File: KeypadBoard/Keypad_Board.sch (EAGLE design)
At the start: 31 parts, among them Q1 4.3A/20V/54mΩ, U1 ESP32-WROOM-32E_(16MB), U2 LTC1730ES8-4.2#TRPBF

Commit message: Board Rev2
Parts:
- added J8: (no value), SparkFun-Connectors:CONN_05
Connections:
- new net BTN1: J8.3, U1.IO15
- new net X_AXIS: J8.5, U1.IO34
- new net Y_AXIS: J8.4, U1.IO35
- net 3V3: now also J8.1
- net GND: now also J8.2
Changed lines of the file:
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@@
 <part name="SUPPLY10" library="supply2" library_urn="urn:adsk.eagle:library:372" deviceset="GND" device=""/>
 <part name="J7" library="SparkFun-Connectors" library_urn="urn:adsk.eagle:library:513" deviceset="CONN_02" device="" package3d_urn="urn:adsk.eagle:package:38039/1"/>
+<part name="J8" library="SparkFun-Connectors" library_urn="urn:adsk.eagle:library:513" deviceset="CONN_05" device="" package3d_urn="urn:adsk.eagle:package:38104/1"/>
 </parts>
 <sheets>
@@
 <attribute name="NAME" x="66.04" y="104.648" size="1.778" layer="95" font="vector"/>
 </instance>
+<instance part="J8" gate="G$1" x="325.12" y="45.72" smashed="yes" rot="R180">
+<attribute name="VALUE" x="327.66" y="55.626" size="1.778" layer="96" font="vector" rot="R180"/>
+<attribute name="NAME" x="327.66" y="37.592" size="1.778" layer="95" font="vector" rot="R180"/>
+</instance>
 </instances>
 <busses>
@@
 <pinref part="SUPPLY10" gate="GND" pin="GND"/>
 <wire x1="294.64" y1="137.16" x2="294.64" y2="132.08" width="0.1524" layer="91"/>
+</segment>
+<segment>
+<pinref part="J8" gate="G$1" pin="2"/>
+<wire x1="317.5" y1="48.26" x2="307.34" y2="48.26" width="0.1524" layer="91"/>
+<label x="307.34" y="48.26" size="1.778" layer="95"/>
 </segment>
 </net>
@@
 <label x="271.78" y="83.82" size="1.778" layer="95"/>
 </segment>
+<segment>
+<pinref part="J8" gate="G$1" pin="1"/>
+<wire x1="317.5" y1="50.8" x2="307.34" y2="50.8" width="0.1524" layer="91"/>
+<label x="307.34" y="50.8" size="1.778" layer="95"/>
+</segment>
 </net>
 <net name="N$9" class="0">
@@
 </segment>
 </net>
+<net name="X_AXIS" class="0">
+<segment>
+<pinref part="J8" gate="G$1" pin="5"/>
+<wire x1="317.5" y1="40.64" x2="307.34" y2="40.64" width="0.1524" layer="91"/>
+<label x="307.34" y="40.64" size="1.778" layer="95"/>
+</segment>
+<segment>
+<pinref part="U1" gate="G$1" pin="IO34"/>
+<wire x1="233.68" y1="121.92" x2="223.52" y2="121.92" width="0.1524" layer="91"/>
+<label x="223.52" y="121.92" size="1.778" layer="95"/>
+</segment>
+</net>
+<net name="Y_AXIS" class="0">
+<segment>
+<pinref part="J8" gate="G$1" pin="4"/>
+<wire x1="317.5" y1="43.18" x2="307.34" y2="43.18" width="0.1524" layer="91"/>
+<label x="307.34" y="43.18" size="1.778" layer="95"/>
+</segment>
+<segment>
+<pinref part="U1" gate="G$1" pin="IO35"/>
+<wire x1="233.68" y1="119.38" x2="223.52" y2="119.38" width="0.1524" layer="91"/>
+<label x="223.52" y="119.38" size="1.778" layer="95"/>
+</segment>
+</net>
+<net name="BTN1" class="0">
+<segment>
+<pinref part="J8" gate="G$1" pin="3"/>
+<wire x1="317.5" y1="45.72" x2="307.34" y2="45.72" width="0.1524" layer="91"/>
+<label x="307.34" y="45.72" size="1.778" layer="95"/>
+</segment>
+<segment>
+<pinref part="U1" gate="G$1" pin="IO15"/>
+<wire x1="274.32" y1="132.08" x2="284.48" y2="132.08" width="0.1524" layer="91"/>
+<label x="276.86" y="132.08" size="1.778" layer="95"/>
+</segment>
+</net>

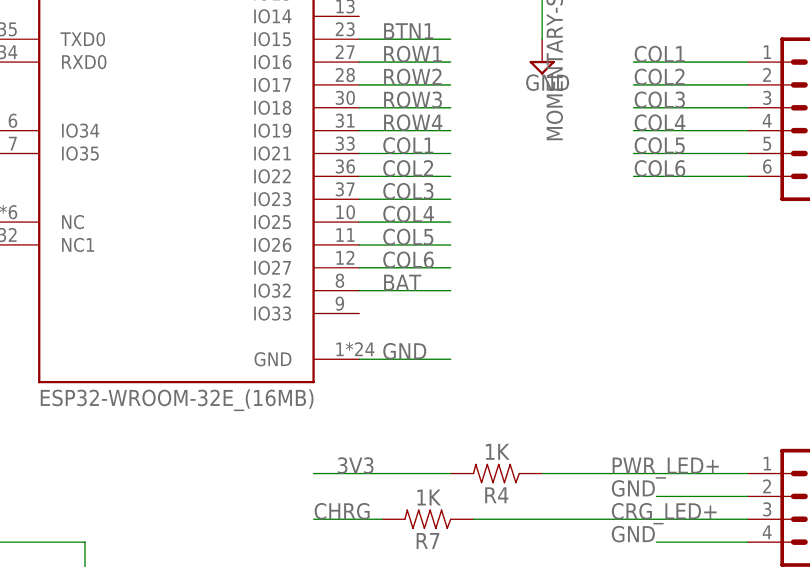
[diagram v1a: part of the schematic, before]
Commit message: Board updates - ADC OverVoltage fix
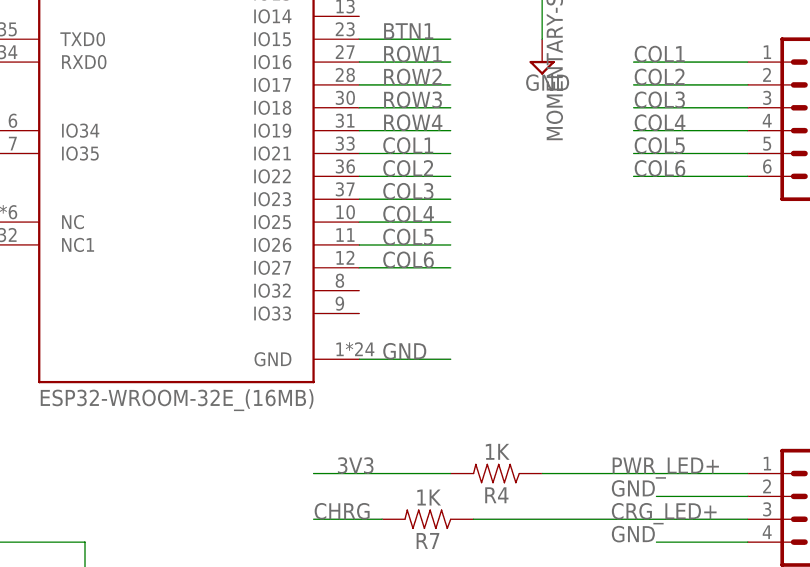
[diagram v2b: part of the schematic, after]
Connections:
- net BAT: no longer U1.IO32
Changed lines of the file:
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@@
 <net name="BAT" class="0">
-<segment>
-<pinref part="U1" gate="G$1" pin="IO32"/>
-<wire x1="274.32" y1="104.14" x2="284.48" y2="104.14" width="0.1524" layer="91"/>
-<label x="276.86" y="104.14" size="1.778" layer="95"/>
-</segment>
 <segment>
 <pinref part="U2" gate="G$1" pin="BAT"/>

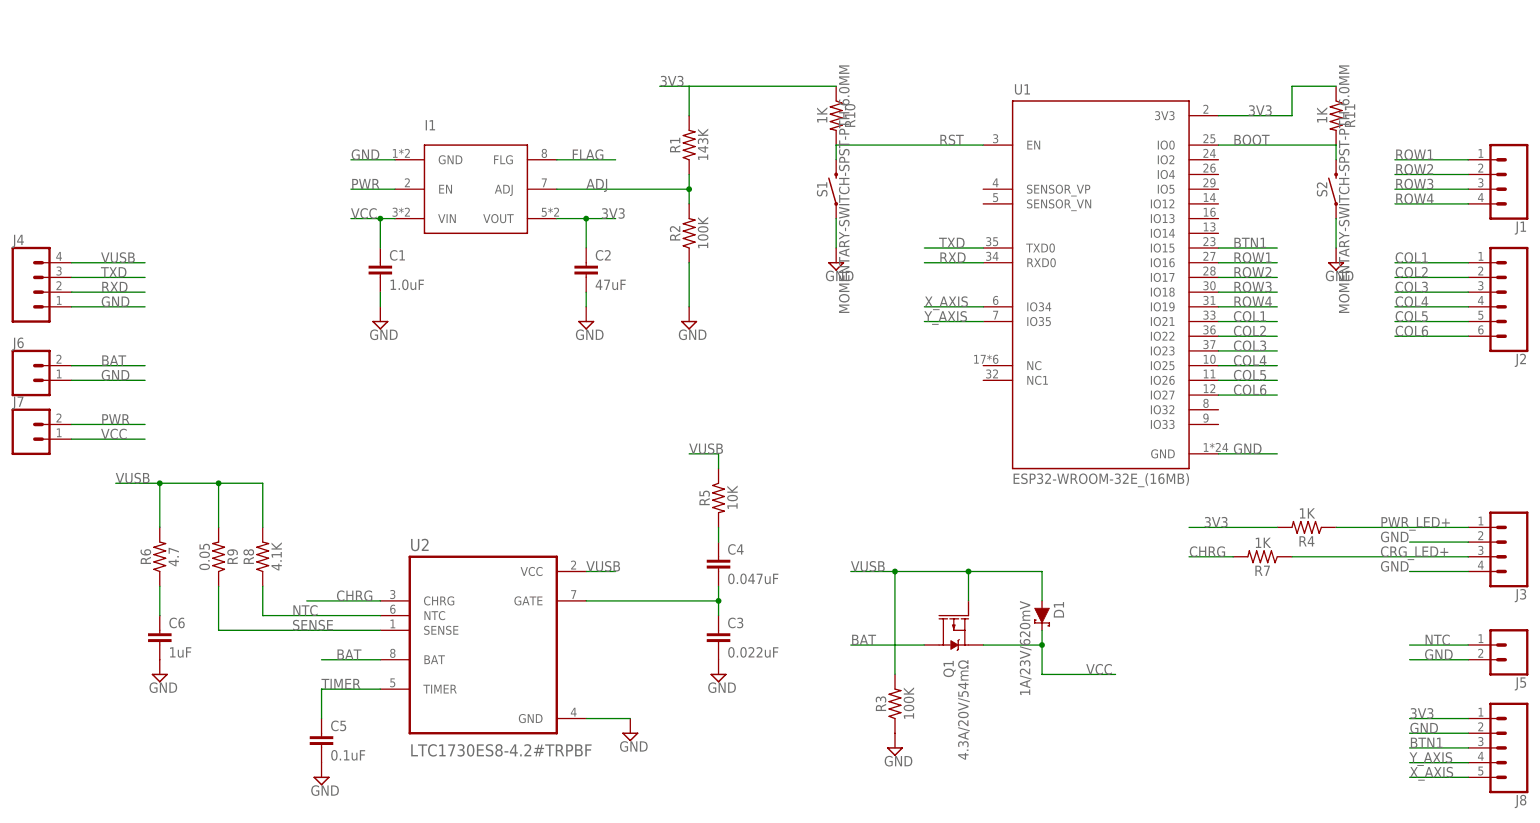
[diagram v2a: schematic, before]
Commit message: Added battery level monitoring and charge LED
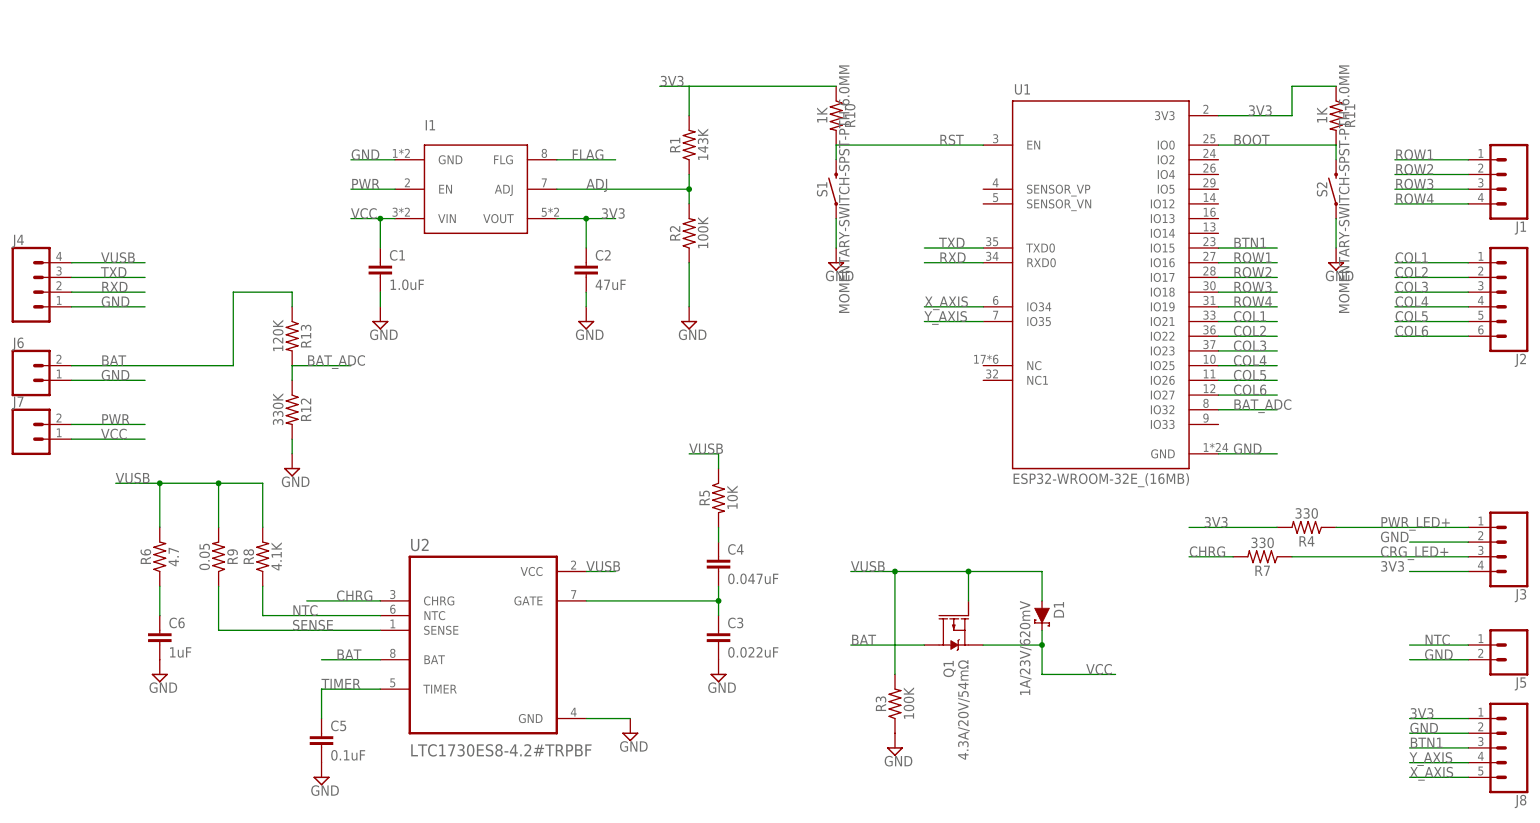
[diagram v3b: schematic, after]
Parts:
- added R12: 330K, SparkFun-Resistors:0.22OHM-0805-1/4W-1%
- added R13: 120K, SparkFun-Resistors:0.22OHM-0805-1/4W-1%
- R4, R7: value 1K -> 330
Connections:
- new net BAT_ADC: R12.1, R13.2, U1.IO32
- net 3V3: now also J3.4
- net BAT: now also R13.1
- net GND: now also R12.2; no longer J3.4
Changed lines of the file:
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@@
 <part name="C5" library="SparkFun-Capacitors" library_urn="urn:adsk.eagle:library:510" deviceset="0.22UF" device="-0603-50V-(-20/+80%)" package3d_urn="urn:adsk.eagle:package:37414/1" value="0.1uF"/>
 <part name="C6" library="SparkFun-Capacitors" library_urn="urn:adsk.eagle:library:510" deviceset="0.22UF" device="-0603-50V-(-20/+80%)" package3d_urn="urn:adsk.eagle:package:37414/1" value="1uF"/>
-<part name="R4" library="SparkFun-Resistors" library_urn="urn:adsk.eagle:library:532" deviceset="0.22OHM" device="-0805-1/4W-1%" package3d_urn="urn:adsk.eagle:package:39651/1" value="1K"/>
+<part name="R4" library="SparkFun-Resistors" library_urn="urn:adsk.eagle:library:532" deviceset="0.22OHM" device="-0805-1/4W-1%" package3d_urn="urn:adsk.eagle:package:39651/1" value="330"/>
 <part name="R5" library="SparkFun-Resistors" library_urn="urn:adsk.eagle:library:532" deviceset="0.22OHM" device="-0805-1/4W-1%" package3d_urn="urn:adsk.eagle:package:39651/1" value="10K"/>
 <part name="R6" library="SparkFun-Resistors" library_urn="urn:adsk.eagle:library:532" deviceset="0.05OHM" device="-0603-1/5W-1%" package3d_urn="urn:adsk.eagle:package:39650/1" value="4.7"/>
@@
 <part name="J4" library="SparkFun-Connectors" library_urn="urn:adsk.eagle:library:513" deviceset="CONN_04" device="" package3d_urn="urn:adsk.eagle:package:38085/1"/>
 <part name="J6" library="SparkFun-Connectors" library_urn="urn:adsk.eagle:library:513" deviceset="CONN_02" device="" package3d_urn="urn:adsk.eagle:package:38039/1"/>
-<part name="R7" library="SparkFun-Resistors" library_urn="urn:adsk.eagle:library:532" deviceset="0.22OHM" device="-0805-1/4W-1%" package3d_urn="urn:adsk.eagle:package:39651/1" value="1K"/>
+<part name="R7" library="SparkFun-Resistors" library_urn="urn:adsk.eagle:library:532" deviceset="0.22OHM" device="-0805-1/4W-1%" package3d_urn="urn:adsk.eagle:package:39651/1" value="330"/>
 <part name="R10" library="SparkFun-Resistors" library_urn="urn:adsk.eagle:library:532" deviceset="0.22OHM" device="-0805-1/4W-1%" package3d_urn="urn:adsk.eagle:package:39651/1" value="1K"/>
 <part name="R11" library="SparkFun-Resistors" library_urn="urn:adsk.eagle:library:532" deviceset="0.22OHM" device="-0805-1/4W-1%" package3d_urn="urn:adsk.eagle:package:39651/1" value="1K"/>
@@
 <part name="J7" library="SparkFun-Connectors" library_urn="urn:adsk.eagle:library:513" deviceset="CONN_02" device="" package3d_urn="urn:adsk.eagle:package:38039/1"/>
 <part name="J8" library="SparkFun-Connectors" library_urn="urn:adsk.eagle:library:513" deviceset="CONN_05" device="" package3d_urn="urn:adsk.eagle:package:38104/1"/>
+<part name="R12" library="SparkFun-Resistors" library_urn="urn:adsk.eagle:library:532" deviceset="0.22OHM" device="-0805-1/4W-1%" package3d_urn="urn:adsk.eagle:package:39651/1" value="330K"/>
+<part name="R13" library="SparkFun-Resistors" library_urn="urn:adsk.eagle:library:532" deviceset="0.22OHM" device="-0805-1/4W-1%" package3d_urn="urn:adsk.eagle:package:39651/1" value="120K"/>
+<part name="SUPPLY11" library="supply2" library_urn="urn:adsk.eagle:library:372" deviceset="GND" device=""/>
 </parts>
 <sheets>
@@
 <attribute name="NAME" x="327.66" y="37.592" size="1.778" layer="95" font="vector" rot="R180"/>
 </instance>
+<instance part="R12" gate="G$1" x="114.3" y="104.14" smashed="yes" rot="R270">
+<attribute name="NAME" x="115.824" y="104.14" size="1.778" layer="95" font="vector" rot="R270" align="bottom-center"/>
+<attribute name="VALUE" x="112.776" y="104.14" size="1.778" layer="96" font="vector" rot="R270" align="top-center"/>
+</instance>
+<instance part="R13" gate="G$1" x="114.3" y="116.84" smashed="yes" rot="R270">
+<attribute name="NAME" x="115.824" y="116.84" size="1.778" layer="95" font="vector" rot="R270" align="bottom-center"/>
+<attribute name="VALUE" x="112.776" y="116.84" size="1.778" layer="96" font="vector" rot="R270" align="top-center"/>
+</instance>
+<instance part="SUPPLY11" gate="GND" x="114.3" y="93.98" smashed="yes">
+<attribute name="VALUE" x="112.395" y="90.805" size="1.778" layer="96"/>
+</instance>
 </instances>
 <busses>
@@
 </segment>
 <segment>
-<pinref part="J3" gate="G$1" pin="4"/>
-<wire x1="317.5" y1="76.2" x2="307.34" y2="76.2" width="0.1524" layer="91"/>
-<label x="302.26" y="76.2" size="1.778" layer="95"/>
-</segment>
-<segment>
 <pinref part="SUPPLY9" gate="GND" pin="GND"/>
 <pinref part="S1" gate="G$1" pin="1"/>
@@
 <label x="307.34" y="48.26" size="1.778" layer="95"/>
 </segment>
+<segment>
+<pinref part="SUPPLY11" gate="GND" pin="GND"/>
+<pinref part="R12" gate="G$1" pin="2"/>
+<wire x1="114.3" y1="96.52" x2="114.3" y2="99.06" width="0.1524" layer="91"/>
+</segment>
 </net>
 <net name="BAT" class="0">
@@
 <segment>
 <pinref part="J6" gate="G$1" pin="2"/>
-<wire x1="76.2" y1="111.76" x2="88.9" y2="111.76" width="0.1524" layer="91"/>
 <label x="81.28" y="111.76" size="1.778" layer="95"/>
+<pinref part="R13" gate="G$1" pin="1"/>
+<wire x1="114.3" y1="121.92" x2="114.3" y2="124.46" width="0.1524" layer="91"/>
+<wire x1="114.3" y1="124.46" x2="104.14" y2="124.46" width="0.1524" layer="91"/>
+<wire x1="104.14" y1="124.46" x2="104.14" y2="111.76" width="0.1524" layer="91"/>
+<wire x1="104.14" y1="111.76" x2="76.2" y2="111.76" width="0.1524" layer="91"/>
 </segment>
 </net>
@@
 <label x="307.34" y="50.8" size="1.778" layer="95"/>
 </segment>
+<segment>
+<pinref part="J3" gate="G$1" pin="4"/>
+<wire x1="317.5" y1="76.2" x2="307.34" y2="76.2" width="0.1524" layer="91"/>
+<label x="302.26" y="76.2" size="1.778" layer="95"/>
+</segment>
 </net>
 <net name="N$9" class="0">
@@
 </segment>
 </net>
+<net name="BAT_ADC" class="0">
+<segment>
+<pinref part="R12" gate="G$1" pin="1"/>
+<pinref part="R13" gate="G$1" pin="2"/>
+<wire x1="114.3" y1="109.22" x2="114.3" y2="111.76" width="0.1524" layer="91"/>
+<wire x1="114.3" y1="111.76" x2="124.46" y2="111.76" width="0.1524" layer="91"/>
+<label x="116.84" y="111.76" size="1.778" layer="95"/>
+</segment>
+<segment>
+<pinref part="U1" gate="G$1" pin="IO32"/>
+<wire x1="274.32" y1="104.14" x2="284.48" y2="104.14" width="0.1524" layer="91"/>
+<label x="276.86" y="104.14" size="1.778" layer="95"/>
+</segment>
+</net>
